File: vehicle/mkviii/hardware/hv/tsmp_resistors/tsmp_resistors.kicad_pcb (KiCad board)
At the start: 2 copper layers, 43.5 x 38.8 mm, 11 parts, among them J1 TS, J2 MP

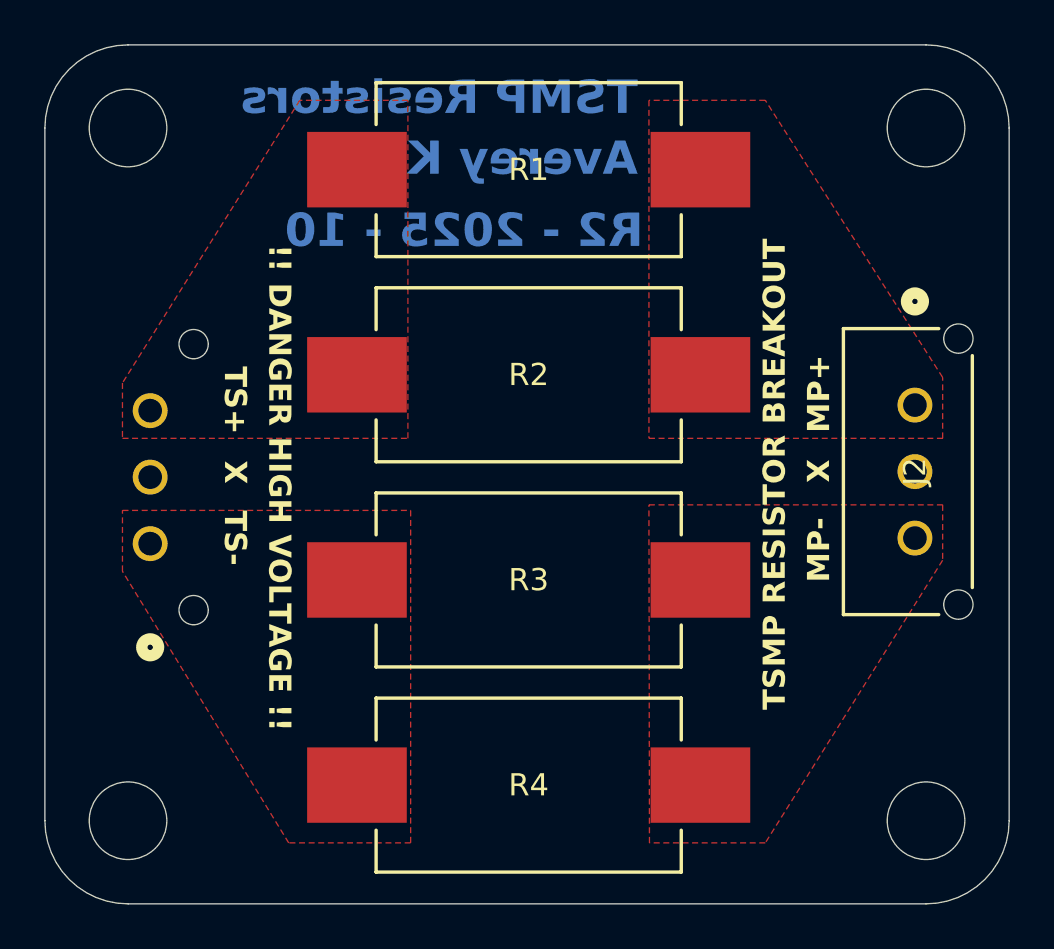
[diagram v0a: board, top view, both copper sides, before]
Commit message: fixed connector being on the back. oops :p
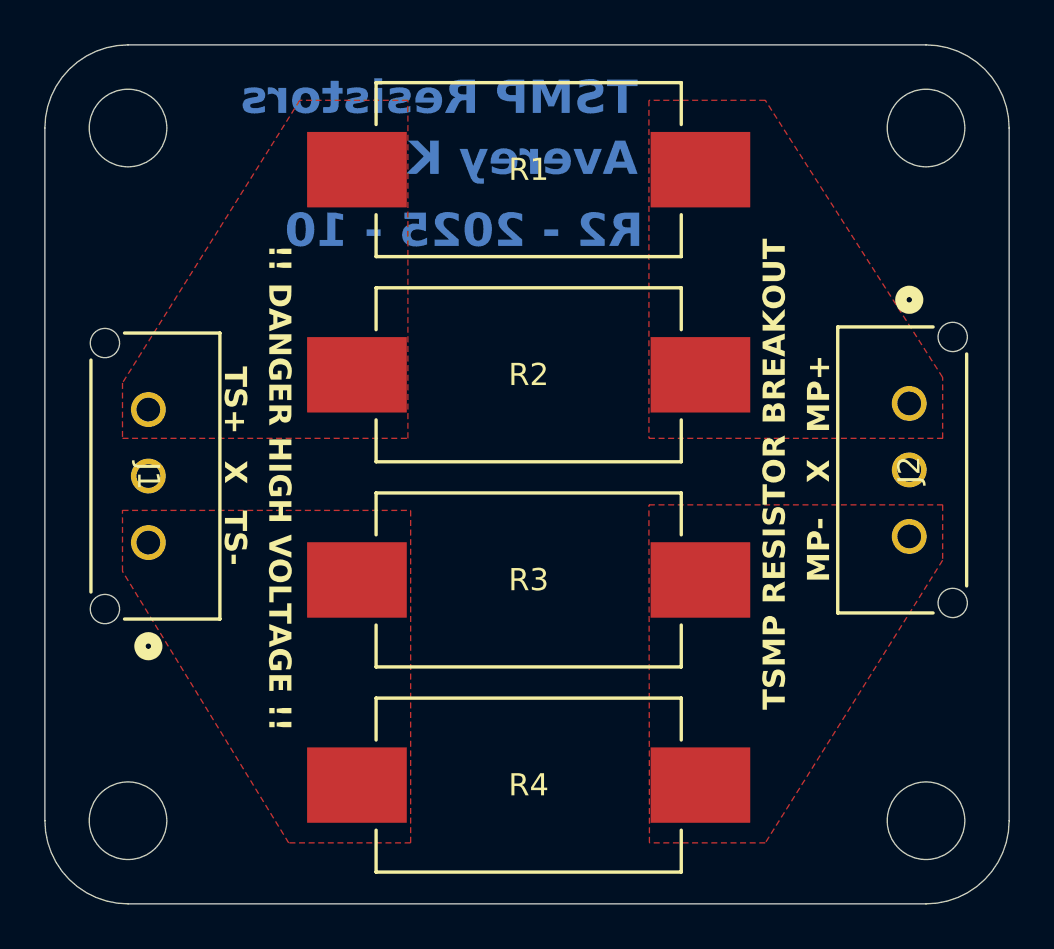
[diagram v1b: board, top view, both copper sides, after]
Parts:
- J1: moved to F.Cu
- moved J2 0.27 mm to (114.0, 99.2)
- moved J1 0.10 mm to (79.7, 105.5)
